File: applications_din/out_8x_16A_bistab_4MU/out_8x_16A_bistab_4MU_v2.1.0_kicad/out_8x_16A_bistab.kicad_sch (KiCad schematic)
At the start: 30 parts, among them IC1 ULN2803, IC2 ULN2803, K1 HFE20-1-024-1HD504, K2 HFE20-1-024-1HD504, K3 HFE20-1-024-1HD504, K4 HFE20-1-024-1HD504, K5 HFE20-1-024-1HD504, K6 HFE20-1-024-1HD504, K7 HFE20-1-024-1HD504, K8 HFE20-1-024-1HD504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

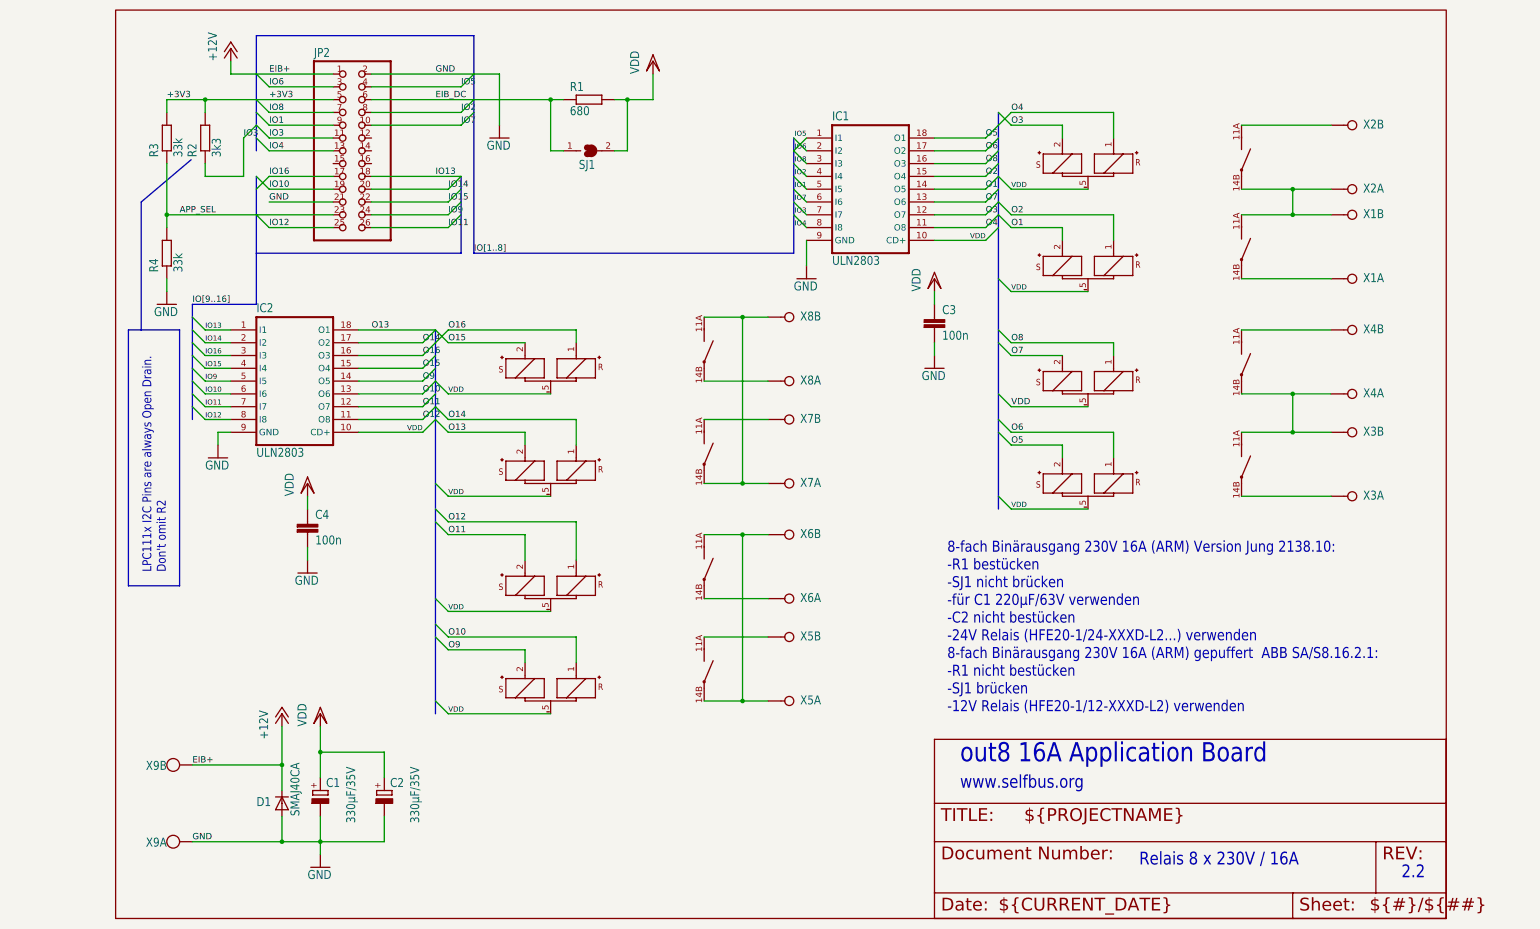
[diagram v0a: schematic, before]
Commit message: rename and move out 8x 16A bistab 2.1 kicad
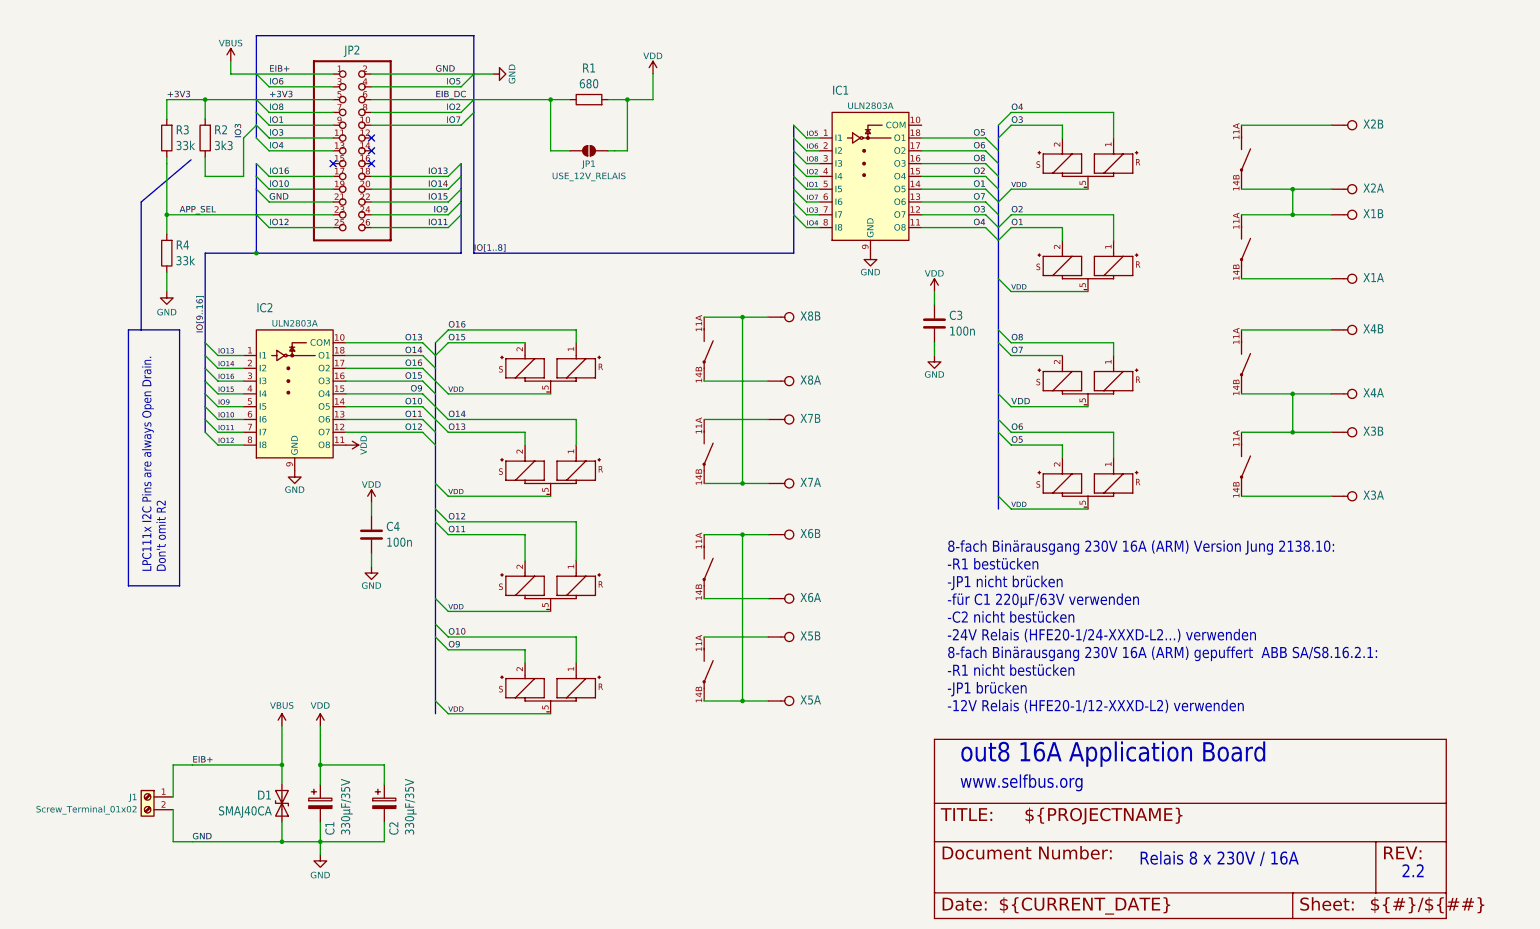
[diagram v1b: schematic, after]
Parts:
- removed X9: W237-102, app_out_8x_16A_bistab_4MU_BOT_v2.0.0:W237-102, symbol app_out_8x_16A_bistab_4MU_BOT_v2.0.0-eagle-import:W237-102
- added J1: Screw_Terminal_01x02, symbol Connector:Screw_Terminal_01x02
- C1, C2: footprint app_out_8x_16A_bistab_4MU_BOT_v2.0.0:E3,5-8 -> out_8x_16A_bistab:E3,5-8; symbol app_out_8x_16A_bistab_4MU_BOT_v2.0.0-eagle-import:CPOL-EUE3.5-8 -> Device:C_Polarized
- C3, C4: footprint app_out_8x_16A_bistab_4MU_BOT_v2.0.0:C1206 -> out_8x_16A_bistab:C1206; symbol app_out_8x_16A_bistab_4MU_BOT_v2.0.0-eagle-import:C-EUC1206 -> Device:C
- D1: footprint app_out_8x_16A_bistab_4MU_BOT_v2.0.0:SMB -> Diode_SMD:D_SMA; symbol app_out_8x_16A_bistab_4MU_BOT_v2.0.0-eagle-import:D-SMB -> Diode:SMAJ40CA
- IC1, IC2: value ULN2803 -> ULN2803A; footprint app_out_8x_16A_bistab_4MU_BOT_v2.0.0:SO18W -> out_8x_16A_bistab:SO18W; symbol app_out_8x_16A_bistab_4MU_BOT_v2.0.0-eagle-import:ULN2803ASOP18 -> Transistor_Array:ULN2803A
- JP1: renamed from SJ1; value A -> USE_12V_RELAIS; symbol app_out_8x_16A_bistab_4MU_BOT_v2.0.0-eagle-import:SJ -> Jumper:SolderJumper_2_Open; now left out of the parts list
- JP2: footprint app_out_8x_16A_bistab_4MU_BOT_v2.0.0:2X13SMD -> out_8x_16A_bistab:2X13SMD; symbol app_out_8x_16A_bistab_4MU_BOT_v2.0.0-eagle-import:PINHD-2X13_2.54-SMD -> out_8x_16A_bistab-eagle-import:PINHD-2X13_2.54-SMD
- K1, K2, K3, K4, K5, K6, K7, K8: footprint app_out_8x_16A_bistab_4MU_BOT_v2.0.0:HFE20-3-504 -> out_8x_16A_bistab:HFE20-3-504; symbol app_out_8x_16A_bistab_4MU_BOT_v2.0.0-eagle-import:HFE20-1-024-1HD504 -> out_8x_16A_bistab-eagle-import:HFE20-1-024-1HD504
- R1, R2, R3, R4: footprint app_out_8x_16A_bistab_4MU_BOT_v2.0.0:M1206 -> out_8x_16A_bistab:M1206; symbol app_out_8x_16A_bistab_4MU_BOT_v2.0.0-eagle-import:R-EU_M1206 -> Device:R
- X1, X2, X3, X4, X5, X6, X7, X8: footprint app_out_8x_16A_bistab_4MU_BOT_v2.0.0:W237-132 -> out_8x_16A_bistab:W237-132; symbol app_out_8x_16A_bistab_4MU_BOT_v2.0.0-eagle-import:W237-02P -> out_8x_16A_bistab-eagle-import:W237-02P
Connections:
- net GND: now also C1.2, C2.2, D1.1 (A1), J1.2 (Pin_2); no longer C1.-, C2.-, D1.2 (A)
- net O10: now also IC2.14 (O5); no longer IC2.13 (O6)
- net O11: now also IC2.13 (O6); no longer IC2.12 (O7)
- net O12: now also IC2.12 (O7); no longer IC2.11 (O8)
- net O13: now also IC2.10 (COM); no longer IC2.18 (O1)
- net O14: now also IC2.18 (O1); no longer IC2.17 (O2)
- net O15: now also IC2.16 (O3); no longer IC2.15 (O4)
- net O16: now also IC2.17 (O2); no longer IC2.16 (O3)
- net O9: now also IC2.15 (O4); no longer IC2.14 (O5)
- net VDD: now also C1.1, C2.1, IC2.11 (O8); no longer C1.+, C2.+, IC1.10 (CD+), IC2.10 (CD+)
- net +12V renamed VBUS
- net VBUS: now also D1.2 (A2), J1.1 (Pin_1); no longer D1.1 (C)
- no-connect marks 0 -> 4
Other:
- note added: "8-fach Binärausgang 230V 16A (ARM) Version Jung 2138.10: -R1 bestücken -JP1 nicht brücken -für C1 220µF/63V verwenden -C2 nicht bestücken -24V Relais (HFE20-1/24-XXXD-L2...) verwenden 8-fach Binärausgang 230V 16A (ARM) gepuffert ABB SA/S8.16.2.1: -R1 nicht bestücken -JP1 brücken -12V Relais (HFE20-1/12-XXXD-L2) verwenden"
- note removed: "8-fach Binärausgang 230V 16A (ARM) Version Jung 2138.10: -R1 bestücken -SJ1 nicht brücken -für C1 220µF/63V verwenden -C2 nicht bestücken -24V Relais (HFE20-1/24-XXXD-L2...) verwenden 8-fach Binärausgang 230V 16A (ARM) gepuffert ABB SA/S8.16.2.1: -R1 nicht bestücken -SJ1 brücken -12V Relais (HFE20-1/12-XXXD-L2) verwenden"
- moved on the sheet: JP1
